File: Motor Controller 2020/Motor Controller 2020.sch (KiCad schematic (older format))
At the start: 44 parts, among them J1 Batt+, J2 Batt-, J3 Input, J4 Motor+, J5 Motor-, Q1 IRF1404, Q2 IRF1404, Q3 IRF1404, Q4 IRF1404, Q5 IRF1404, Q6 IRF1404, Q7 IRF1404, Q8 IRF1404, SW1 SW_DIP_x03, U1 MAX15062A, U2 a4956, U3 Attiny4313

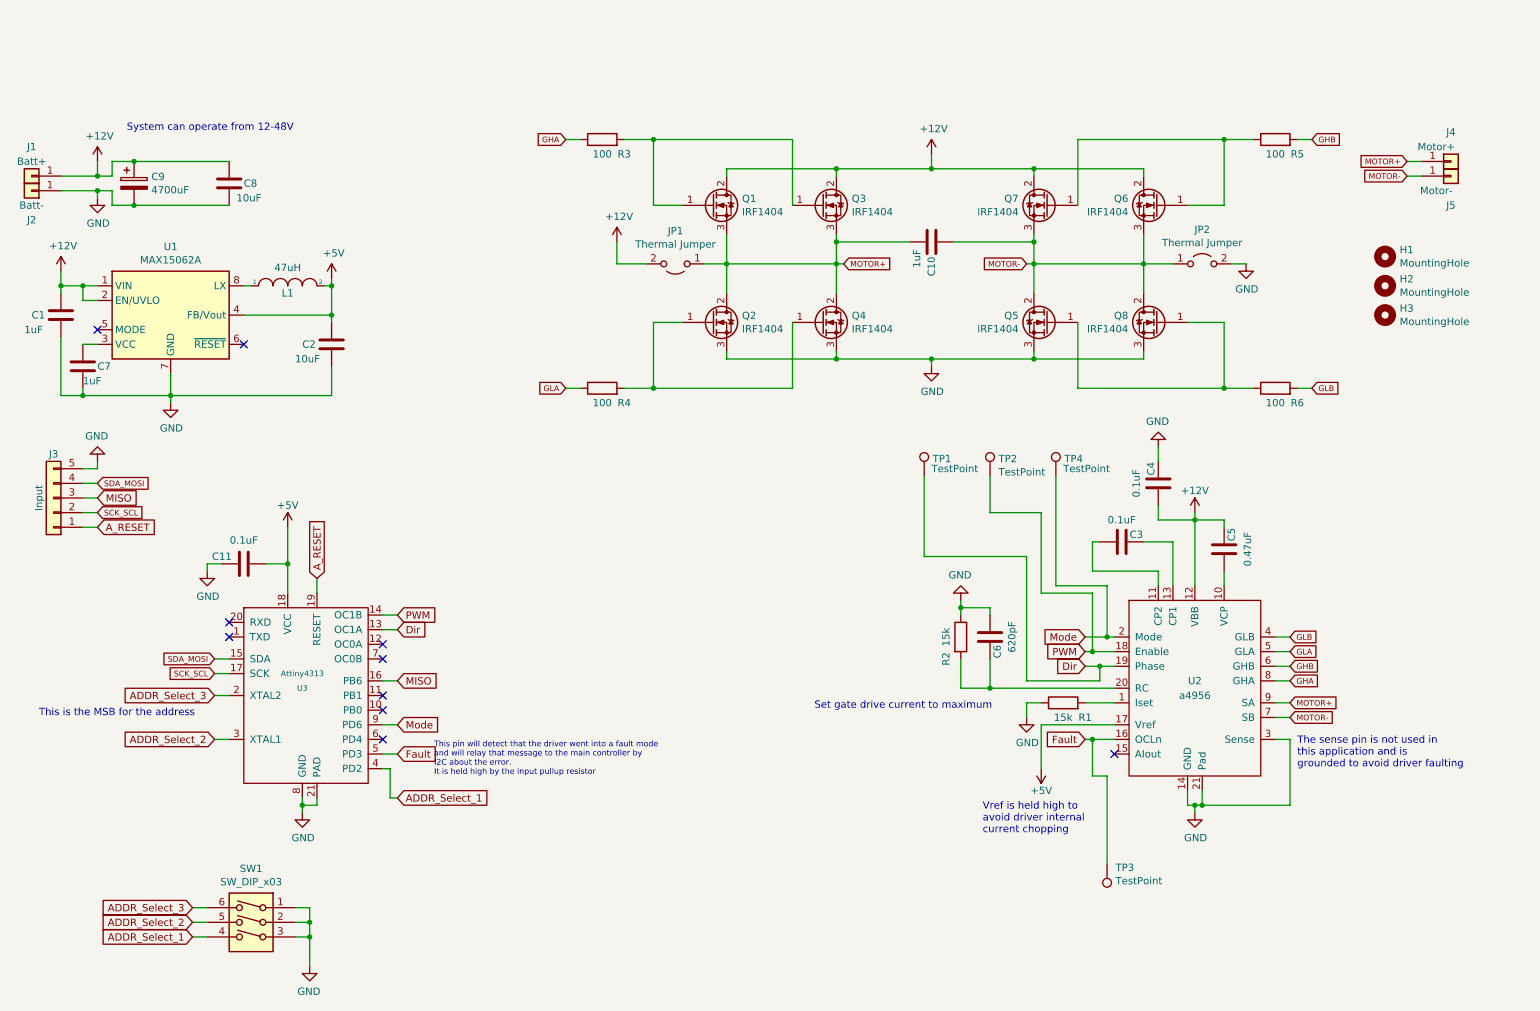
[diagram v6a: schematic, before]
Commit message: Updated Controller board
Separated the logic and power GNDs to minimize noise. Added more Vias for current capability. Rerouted MOSFET tracks to be nearly the same length. Filleted the corners on copper pours. Added more test points for diagnosis.
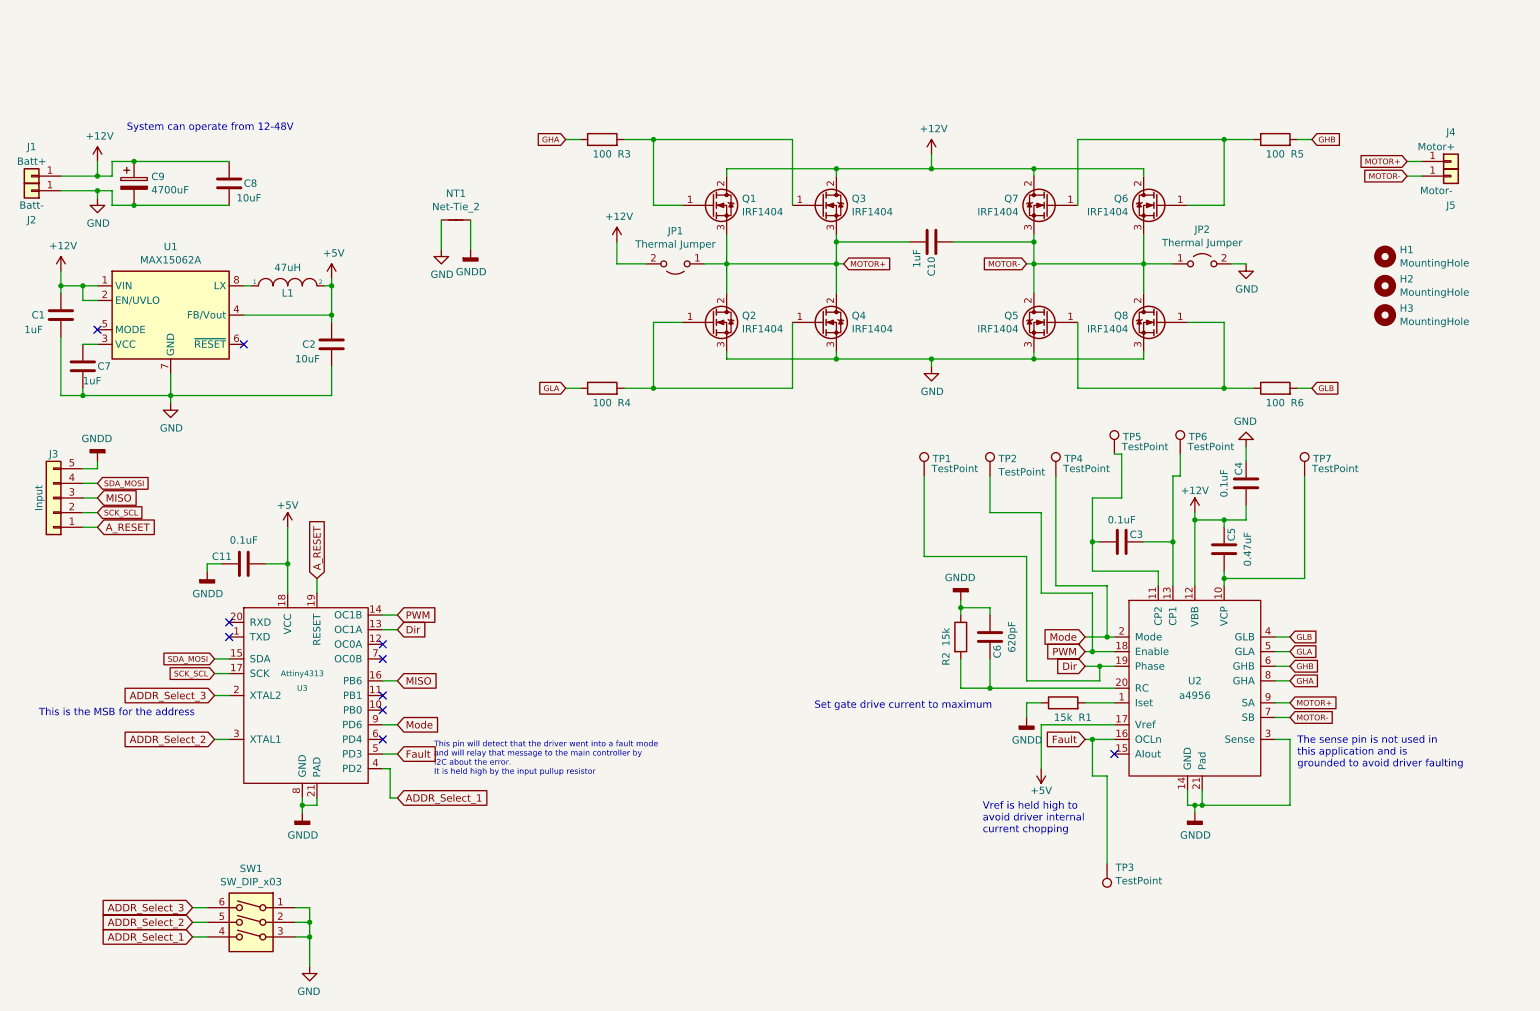
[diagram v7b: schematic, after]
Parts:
- added NT1: Net-Tie_2, NetTie:NetTie-2_SMD_Pad2.0mm, symbol Device:Net-Tie_2
- added TP5, TP6, TP7: TestPoint, TestPoint:TestPoint_Pad_D1.0mm, symbol Connector:TestPoint
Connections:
- net GND: now also NT1.1; no longer C11.1, C6.2, J3.5 (Pin_5), R1.1, R2.1, U2.14 (GND), U2.21 (Pad), U2.3 (Sense), U3.21 (PAD), U3.8 (GND)
- net at C5.2, U2.10 (VCP): now also TP7.1
- net at C3.2, U2.11 (CP2): now also TP5.1
- net at C3.1, U2.13 (CP1): now also TP6.1
- new net GNDD: C11.1, C6.2, J3.5 (Pin_5), NT1.2, R1.1, R2.1, U2.14 (GND), U2.21 (Pad), U2.3 (Sense), U3.21 (PAD), U3.8 (GND)
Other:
- moved on the sheet: C4
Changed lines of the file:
@@
-	1    0    0    -1
-$EndComp
-$Comp
-L power:GND #PWR012
-U 1 1 60BC4FE1
-P 1800 3600
-F 0 "#PWR012" H 1800 3350 50  0001 C CNN
-F 1 "GND" H 1805 3427 50  0000 C CNN
-F 2 "" H 1800 3600 50  0001 C CNN
-F 3 "" H 1800 3600 50  0001 C CNN
-	1    1800 3600
 	1    0    0    -1
 $EndComp
@@
 Text Notes 3350 5000 0    39   ~ 0
 This pin will detect that the driver went into a fault mode \nand will relay that message to the main controller by \nI2C about the error.\nIt is held high by the input pullup resistor
-$Comp
-L power:GND #PWR014
-U 1 1 60BF2F84
-P 2450 5250
-F 0 "#PWR014" H 2450 5000 50  0001 C CNN
-F 1 "GND" H 2455 5077 50  0000 C CNN
-F 2 "" H 2450 5250 50  0001 C CNN
-F 3 "" H 2450 5250 50  0001 C CNN
-	1    2450 5250
-	1    0    0    -1
-$EndComp
 $Comp
 L Connector_Generic:Conn_01x01 J1
@@
 	1    10300 800
 	1    0    0    -1
-$EndComp
-$Comp
-L power:GND #PWR016
-U 1 1 60D499DC
-P 1050 2850
-F 0 "#PWR016" H 1050 2600 50  0001 C CNN
-F 1 "GND" H 1055 2677 50  0000 C CNN
-F 2 "" H 1050 2850 50  0001 C CNN
-F 3 "" H 1050 2850 50  0001 C CNN
-	1    1050 2850
-	-1   0    0    1
 $EndComp
 Text GLabel 1050 3000 2    39   Input ~ 0
@@
 	8550 3200 8550 3250
 Wire Wire Line
-	8750 3600 8750 3700
+	8750 3600 8750 3650
 Wire Wire Line
 	8750 3300 8750 3250
@@
 L Device:C C4
 U 1 1 60B89730
-P 8300 3000
-F 0 "C4" V 8350 3100 50  0000 C CNN
-F 1 "0.1uF" V 8450 3000 50  0000 C CNN
-F 2 "Capacitor_SMD:C_1812_4532Metric_Pad1.57x3.40mm_HandSolder" H 8338 2850 50  0001 C CNN
-F 3 "~" H 8300 3000 50  0001 C CNN
-	1    8300 3000
+P 8900 3000
+F 0 "C4" V 8950 3100 50  0000 C CNN
+F 1 "0.1uF" V 9050 3000 50  0000 C CNN
+F 2 "Capacitor_SMD:C_1812_4532Metric_Pad1.57x3.40mm_HandSolder" H 8938 2850 50  0001 C CNN
+F 3 "~" H 8900 3000 50  0001 C CNN
+	1    8900 3000
 	-1   0    0    -1
 $EndComp
-$Comp
-L power:GND #PWR010
-U 1 1 60B8A336
-P 8300 2750
-F 0 "#PWR010" H 8300 2500 50  0001 C CNN
-F 1 "GND" H 8305 2577 50  0000 C CNN
-F 2 "" H 8300 2750 50  0001 C CNN
-F 3 "" H 8300 2750 50  0001 C CNN
-	1    8300 2750
-	-1   0    0    1
-$EndComp
-Wire Wire Line
-	8300 3150 8300 3250
-Wire Wire Line
-	8300 3250 8550 3250
-Wire Wire Line
-	8300 2850 8300 2750
 $Comp
 L Device:C C3
@@
 Fault
 NoConn ~ 8000 4850
-$Comp
-L power:GND #PWR015
-U 1 1 60BE7979
-P 8550 5250
-F 0 "#PWR015" H 8550 5000 50  0001 C CNN
-F 1 "GND" H 8555 5077 50  0000 C CNN
-F 2 "" H 8550 5250 50  0001 C CNN
-F 3 "" H 8550 5250 50  0001 C CNN
-	1    8550 5250
-	1    0    0    -1
-$EndComp
 Wire Wire Line
 	8600 5100 8600 5200
@@
 Wire Wire Line
 	7800 4500 8000 4500
-$Comp
-L power:GND #PWR08
-U 1 1 60C770C5
-P 7400 4600
-F 0 "#PWR08" H 7400 4350 50  0001 C CNN
-F 1 "GND" H 7405 4427 50  0000 C CNN
-F 2 "" H 7400 4600 50  0001 C CNN
-F 3 "" H 7400 4600 50  0001 C CNN
-	1    7400 4600
-	1    0    0    -1
-$EndComp
 Wire Wire Line
 	7500 4500 7400 4500
@@
 $EndComp
 $Comp
-L power:GND #PWR017
-U 1 1 60C4941C
-P 6950 3800
-F 0 "#PWR017" H 6950 3550 50  0001 C CNN
-F 1 "GND" H 6955 3627 50  0000 C CNN
-F 2 "" H 6950 3800 50  0001 C CNN
-F 3 "" H 6950 3800 50  0001 C CNN
-	1    6950 3800
-	-1   0    0    1
-$EndComp
-$Comp
 L Device:C C6
 U 1 1 60C4FE3E
@@
 Wire Wire Line
 	6100 1350 6100 1500
+$Comp
+L power:GNDD #PWR0103
+U 1 1 60E412FF
+P 1050 2850
+F 0 "#PWR0103" H 1050 2600 50  0001 C CNN
+F 1 "GNDD" H 1054 2695 50  0000 C CNN
+F 2 "" H 1050 2850 50  0001 C CNN
+F 3 "" H 1050 2850 50  0001 C CNN
+	1    1050 2850
+	-1   0    0    1
+$EndComp
+$Comp
+L power:GNDD #PWR0104
+U 1 1 60E423BA
+P 2450 5250
+F 0 "#PWR0104" H 2450 5000 50  0001 C CNN
+F 1 "GNDD" H 2454 5095 50  0000 C CNN
+F 2 "" H 2450 5250 50  0001 C CNN
+F 3 "" H 2450 5250 50  0001 C CNN
+	1    2450 5250
+	1    0    0    -1
+$EndComp
+$Comp
+L power:GNDD #PWR0105
+U 1 1 60E4276C
+P 1800 3600
+F 0 "#PWR0105" H 1800 3350 50  0001 C CNN
+F 1 "GNDD" H 1804 3445 50  0000 C CNN
+F 2 "" H 1800 3600 50  0001 C CNN
+F 3 "" H 1800 3600 50  0001 C CNN
+	1    1800 3600
+	1    0    0    -1
+$EndComp
+$Comp
+L power:GNDD #PWR0106
+U 1 1 60E43F9D
+P 8550 5250
+F 0 "#PWR0106" H 8550 5000 50  0001 C CNN
+F 1 "GNDD" H 8554 5095 50  0000 C CNN
+F 2 "" H 8550 5250 50  0001 C CNN
+F 3 "" H 8550 5250 50  0001 C CNN
+	1    8550 5250
+	1    0    0    -1
+$EndComp
+$Comp
+L power:GNDD #PWR0109
+U 1 1 60E45DA5
+P 7400 4600
+F 0 "#PWR0109" H 7400 4350 50  0001 C CNN
+F 1 "GNDD" H 7404 4445 50  0000 C CNN
+F 2 "" H 7400 4600 50  0001 C CNN
+F 3 "" H 7400 4600 50  0001 C CNN
+	1    7400 4600
+	1    0    0    -1
+$EndComp
+$Comp
+L power:GNDD #PWR0111
+U 1 1 60E876F0
+P 6950 3800
+F 0 "#PWR0111" H 6950 3550 50  0001 C CNN
+F 1 "GNDD" H 6954 3645 50  0000 C CNN
+F 2 "" H 6950 3800 50  0001 C CNN
+F 3 "" H 6950 3800 50  0001 C CNN
+	1    6950 3800
+	-1   0    0    1
+$EndComp
+$Comp
+L power:GND #PWR0107
+U 1 1 60F182EE
+P 8900 2750
+F 0 "#PWR0107" H 8900 2500 50  0001 C CNN
+F 1 "GND" H 8905 2577 50  0000 C CNN
+F 2 "" H 8900 2750 50  0001 C CNN
+F 3 "" H 8900 2750 50  0001 C CNN
+	1    8900 2750
+	-1   0    0    1
+$EndComp
+$Comp
+L power:GND #PWR08
+U 1 1 60F318AF
+P 3400 1400
+F 0 "#PWR08" H 3400 1150 50  0001 C CNN
+F 1 "GND" H 3405 1227 50  0000 C CNN
+F 2 "" H 3400 1400 50  0001 C CNN
+F 3 "" H 3400 1400 50  0001 C CNN
+	1    3400 1400
+	1    0    0    -1
+$EndComp
+$Comp
+L power:GNDD #PWR010
+U 1 1 60F31C6D
+P 3600 1400
+F 0 "#PWR010" H 3600 1150 50  0001 C CNN
+F 1 "GNDD" H 3604 1245 50  0000 C CNN
+F 2 "" H 3600 1400 50  0001 C CNN
+F 3 "" H 3600 1400 50  0001 C CNN
+	1    3600 1400
+	1    0    0    -1
+$EndComp
+$Comp
+L Device:Net-Tie_2 NT1
+U 1 1 60F32F60
+P 3500 1200
+F 0 "NT1" H 3500 1381 50  0000 C CNN
+F 1 "Net-Tie_2" H 3500 1290 50  0000 C CNN
+F 2 "NetTie:NetTie-2_SMD_Pad2.0mm" H 3500 1200 50  0001 C CNN
+F 3 "~" H 3500 1200 50  0001 C CNN
+	1    3500 1200
+	1    0    0    -1
+$EndComp
+Wire Wire Line
+	3600 1200 3600 1400
+Wire Wire Line
+	3400 1200 3400 1400
+Wire Wire Line
+	8750 3250 8900 3250
+Wire Wire Line
+	8900 3250 8900 3150
+Connection ~ 8750 3250
+Wire Wire Line
+	8900 2850 8900 2750
+$Comp
+L Connector:TestPoint TP6
+U 1 1 60F8CF30
+P 8450 2800
+F 0 "TP6" H 8508 2918 50  0000 L CNN
+F 1 "TestPoint" H 8500 2850 50  0000 L CNN
+F 2 "TestPoint:TestPoint_Pad_D1.0mm" H 8650 2800 50  0001 C CNN
+F 3 "~" H 8650 2800 50  0001 C CNN
+	1    8450 2800
+	1    0    0    -1
+$EndComp
+$Comp
+L Connector:TestPoint TP5
+U 1 1 60F8D930
+P 8000 2800
+F 0 "TP5" H 8058 2918 50  0000 L CNN
+F 1 "TestPoint" H 8050 2850 50  0000 L CNN
+F 2 "TestPoint:TestPoint_Pad_D1.0mm" H 8200 2800 50  0001 C CNN
+F 3 "~" H 8200 2800 50  0001 C CNN
+	1    8000 2800
+	1    0    0    -1
+$EndComp
+Wire Wire Line
+	8450 2800 8450 2950
+Wire Wire Line
+	8450 2950 8400 2950
+Wire Wire Line
+	8400 2950 8400 3400
+Connection ~ 8400 3400
+Wire Wire Line
+	8000 2800 8050 2800
+Wire Wire Line
+	8050 2800 8050 3100
+Wire Wire Line
+	8050 3100 7850 3100
+Wire Wire Line
+	7850 3100 7850 3400
+Connection ~ 7850 3400
+$Comp
+L Connector:TestPoint TP7
+U 1 1 60FA77BA
+P 9300 2950
+F 0 "TP7" H 9358 3068 50  0000 L CNN
+F 1 "TestPoint" H 9350 3000 50  0000 L CNN
+F 2 "TestPoint:TestPoint_Pad_D1.0mm" H 9500 2950 50  0001 C CNN
+F 3 "~" H 9500 2950 50  0001 C CNN
+	1    9300 2950
+	1    0    0    -1
+$EndComp
+Wire Wire Line
+	8750 3650 9300 3650
+Wire Wire Line
+	9300 2950 9300 3650
+Connection ~ 8750 3650
+Wire Wire Line
+	8750 3650 8750 3700
 $EndSCHEMATC

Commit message: Updated schematic and PCB
Reduced the loop length to just over half the original length. Added more Vias for stitching. Changed MOSFET to handle up to 48V, meaning that the system can work up to 48V while still maintaining the 65A continuous rating.
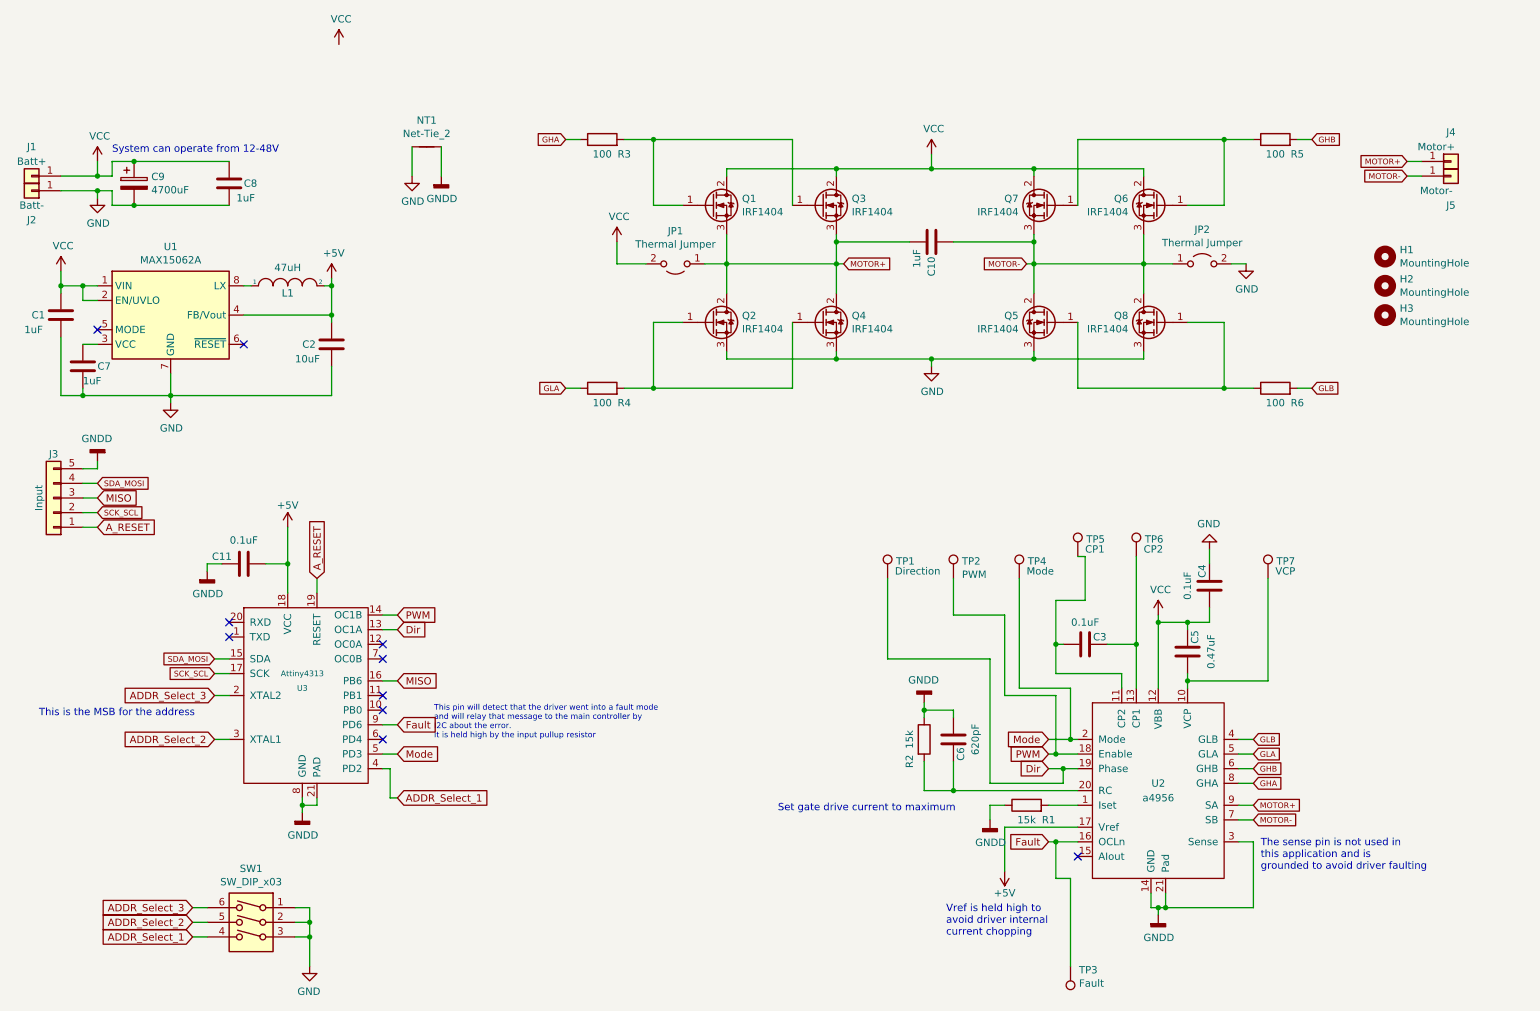
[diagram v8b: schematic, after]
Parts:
- C8: value 10uF -> 1uF
- TP1: value TestPoint -> Direction
- TP2: value TestPoint -> PWM
- TP3: value TestPoint -> Fault
- TP4: value TestPoint -> Mode
- TP5: value TestPoint -> CP1
- TP6: value TestPoint -> CP2
- TP7: value TestPoint -> VCP
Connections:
- net Fault: now also U3.9 (PD6); no longer U3.5 (PD3)
- net Mode: now also U3.5 (PD3); no longer U3.9 (PD6)
- net +12V renamed VCC
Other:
- moved on the sheet: C3, C4, C5, C6, NT1, R1, R2, TP1, TP2, TP3, TP4, TP5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
